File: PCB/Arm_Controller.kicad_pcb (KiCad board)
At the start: 4 copper layers, 198 parts, among them J1 BTN1, J10 STEP_MOTOR_2, J11 STEP_MOTOR_5, J12 STEP_MOTOR_3, J13 STEP_MOTOR_6, J2 CAN SOCKET, J3 EXTN_PWR, J4 FAN1, J5 SWD Header, J6 PWR_BATT, J7 STEP_MOTOR_4, J8 STEP_MOTOR_1, J9 PWR_24V, U1 STM32G431CBT6, U10 TMC2209-LA-T, U2 XL4005E1, U3 NCP1117-3.3_SOT223, U4 ISO1042DWVR, U5 TMC2209-LA-T, U6 TMC2209-LA-T, U7 TMC2209-LA-T, U8 TMC2209-LA-T, U9 TMC2209-LA-T, Y1 8MHz

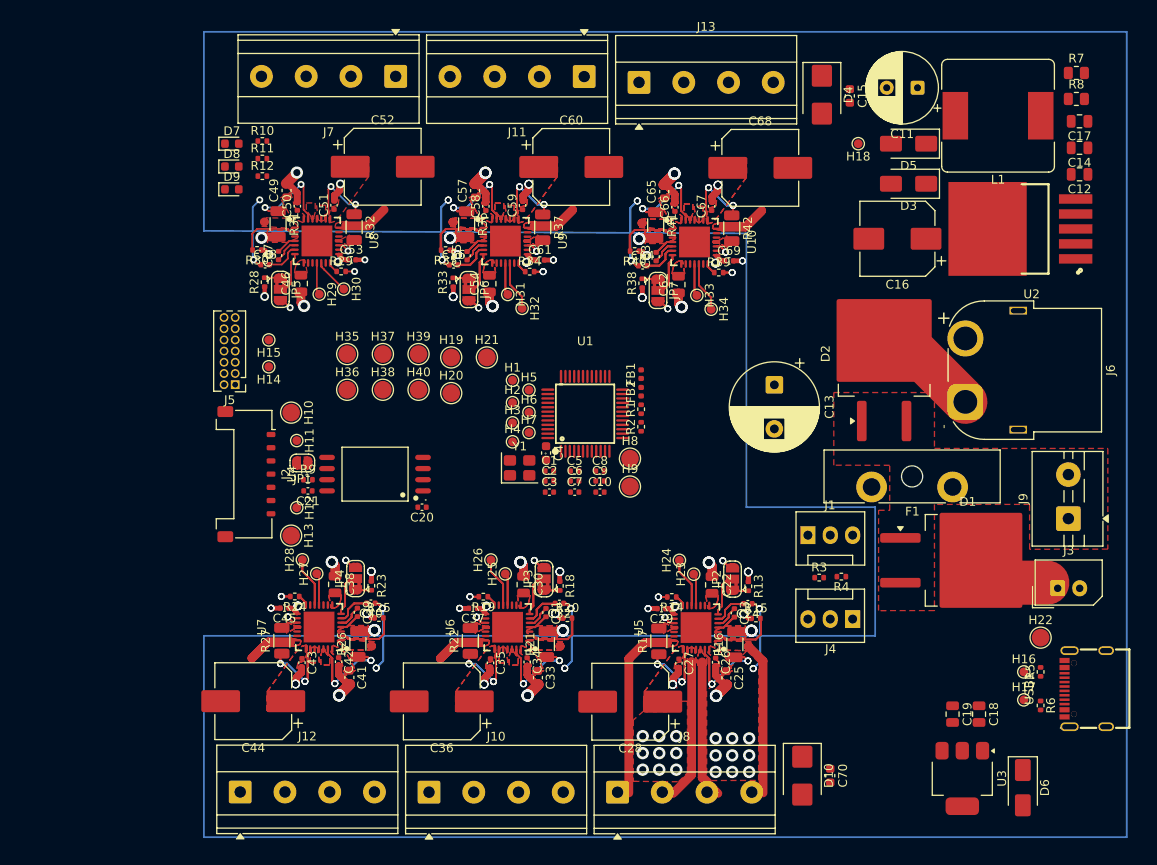
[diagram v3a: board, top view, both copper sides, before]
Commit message: Continued PCB Development - Routed MCU decoupeling and Isolated Crystal - Routed LDO Buck converter (VBUS (+5V) -> +3V3) - Routed Buck Converter (+24V -> +3V3) needs review (U2-pin1-GND) - Started Routing TMC2209 to their terminal blocks - Noticed issue with Stepper Lines coupeling back into +24V - TODO: Move Motor Input farther inside and add grounding isolation - Fixed Polariy mismatch with J3 (XT60 Battery Connector)
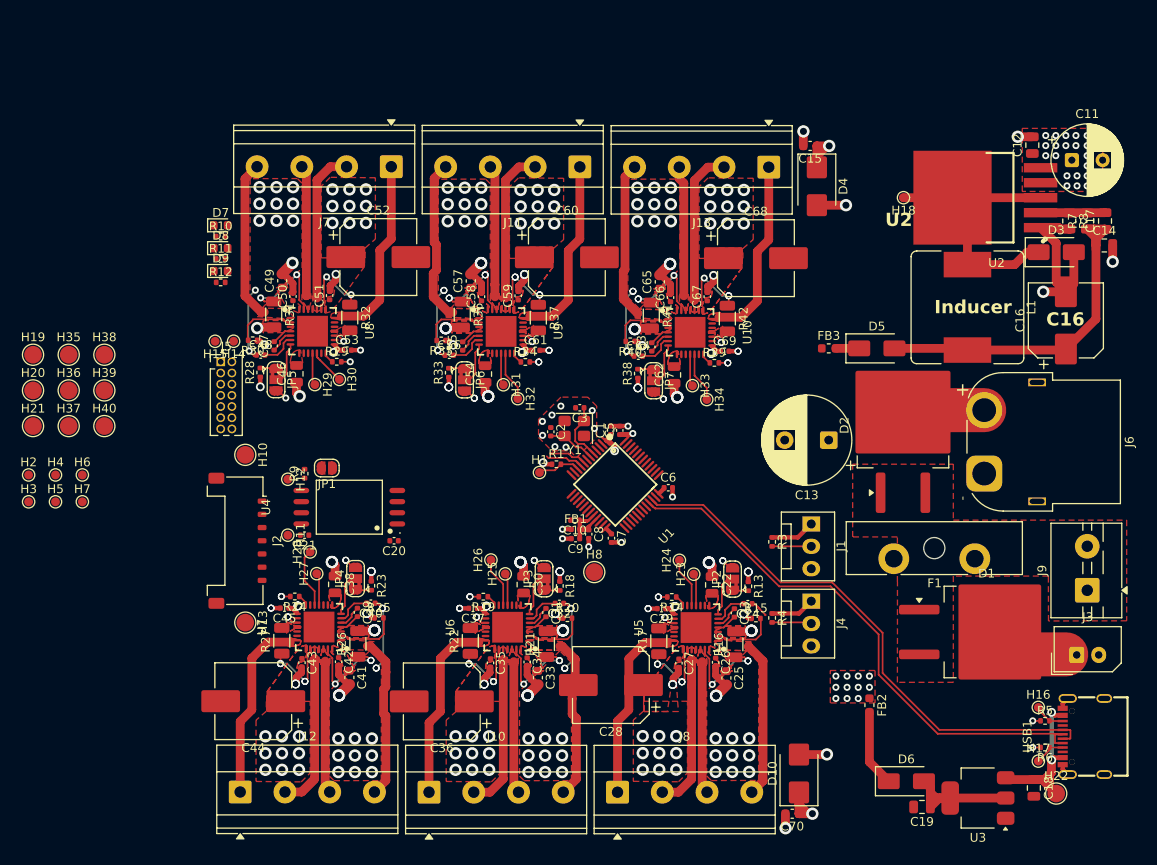
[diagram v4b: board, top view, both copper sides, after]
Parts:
- removed C4: 47uF, Capacitor_SMD:C_0603_1608Metric
- removed H9: VREF+, TestPoint:TestPoint_Pad_D2.0mm
- removed R2: 0R, Resistor_SMD:R_0402_1005Metric
- added FB3: 600R@100MHz, Inductor_SMD:L_0603_1608Metric, F.Cu at (156.7, 81.7)
- C2, C3: value 10pF -> 30pF
- FB1: value 600R@100MHz -> 1kR@100MHz
- FB2: value 1kR@100MHz -> 600R@100MHz; footprint Inductor_SMD:L_0402_1005Metric -> Inductor_SMD:L_0603_1608Metric
- moved H3 55.7 mm to (65.8, 99.1)
- moved H2 55.6 mm to (65.8, 96.0)
- moved H5 55.2 mm to (68.9, 99.1)
- moved H21 52.1 mm to (66.3, 90.5)
- moved H4 52.0 mm to (68.9, 96.0)
- moved H7 51.3 mm to (71.9, 99.1)
- moved H6 51.2 mm to (71.9, 96.0)
- moved H19 47.5 mm to (66.3, 82.4)
- moved H20 47.5 mm to (66.3, 86.4)
- moved FB2 44.0 mm to (161.3, 122.2), turned to -90 degrees
- moved H37 36.6 mm to (70.4, 90.5)
- moved H39 35.9 mm to (74.4, 86.4)
- moved H40 35.9 mm to (74.4, 90.5)
- moved H38 31.9 mm to (74.4, 82.4)
- moved H35 31.6 mm to (70.4, 82.4)
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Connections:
- C10 pad 1: VREF+ -> VDD33A
- C10 pad 2: Net-(C10-Pad2) -> GND
- C5 pad 1: Net-(C4-Pad1) -> +3.3V
- C5 pad 2: Net-(C10-Pad2) -> GND
- C6 pad 1: Net-(C4-Pad1) -> +3.3V
- C6 pad 2: Net-(C10-Pad2) -> GND
- C7 pad 1: Net-(C4-Pad1) -> +3.3V
- C7 pad 2: Net-(C10-Pad2) -> GND
- C8 pad 2: Net-(C10-Pad2) -> GND
- C9 pad 1: Net-(C9-Pad1) -> VDD33A
- C9 pad 2: Net-(C10-Pad2) -> GND
- D5 pad 1: +3.3V -> Net-(D5-K)
- D6 pad 1: +3.3V -> Net-(D6-K)
- FB1 pad 2: Net-(C4-Pad1) -> VDD33A
- FB2 pad 1: Net-(C4-Pad1) -> +3V3
- FB2 pad 2: Net-(C9-Pad1) -> Net-(D6-K)
- J6 pad 1: VBAT -> GND
- J6 pad 2: GND -> VBAT
- U1 pad 20: VREF+ -> VDD33A
- U7 pad 1: TMC1_B2 -> TMC3_B2
- U7 pad 21: TMC1_A2 -> TMC3_A2
- U7 pad 24: TMC1_A1 -> TMC3_A1
- U7 pad 26: TMC1_B1 -> TMC3_B1
- U8 pad 1: TMC1_B2 -> TMC4_B2
- U8 pad 21: TMC1_A2 -> TMC4_A2
- U8 pad 24: TMC1_A1 -> TMC4_A1
- U8 pad 26: TMC1_B1 -> TMC4_B1
- U9 pad 1: TMC1_B2 -> TMC5_B2
- U9 pad 21: TMC1_A2 -> TMC5_A2
- U9 pad 24: TMC1_A1 -> TMC5_A1
- U9 pad 26: TMC1_B1 -> TMC5_B1
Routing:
- net USB_DN: track 0.00 -> 63.2 mm
- net USB_DP: track 0.00 -> 62.8 mm
- net Net-(D5-A): track 0.00 -> 40.0 mm
- net +24V: track 91.1 -> 56.1 mm, vias 40 -> 149
- net Net-(D3-K): track 0.00 -> 32.5 mm
- net GND: track 164.3 -> 133.1 mm, vias 88 -> 109
- net TMC1_A2: track 51.1 -> 20.8 mm
- net VBUS: track 0.00 -> 22.5 mm, vias 0 -> 2
- net (no net): track 0.00 -> 22.1 mm
- net TMC3_A2: track 0.00 -> 20.9 mm
- net TMC4_A2: track 0.00 -> 20.8 mm
- net TMC5_A2: track 0.00 -> 20.8 mm
- net TMC_A_ENN: track 41.5 -> 20.7 mm
- net TMC3_A1: track 0.00 -> 19.6 mm
- net TMC5_B2: track 0.00 -> 18.5 mm
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- added copper zone on In2.Cu, net +24V
- added copper zone on F.Cu, net +3V3
- added copper zone on In2.Cu, net +3V3
- added copper zone on In1.Cu, net GND
- added copper zone on F.Cu, net TMC3_B2
- added copper zone on F.Cu, net TMC5_B2
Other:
- board text added: "C16"
- board text added: "Inducer"
- board text added: "U2"
